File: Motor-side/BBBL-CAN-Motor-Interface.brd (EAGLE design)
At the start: 49.5 x 53.3 mm, 2 parts

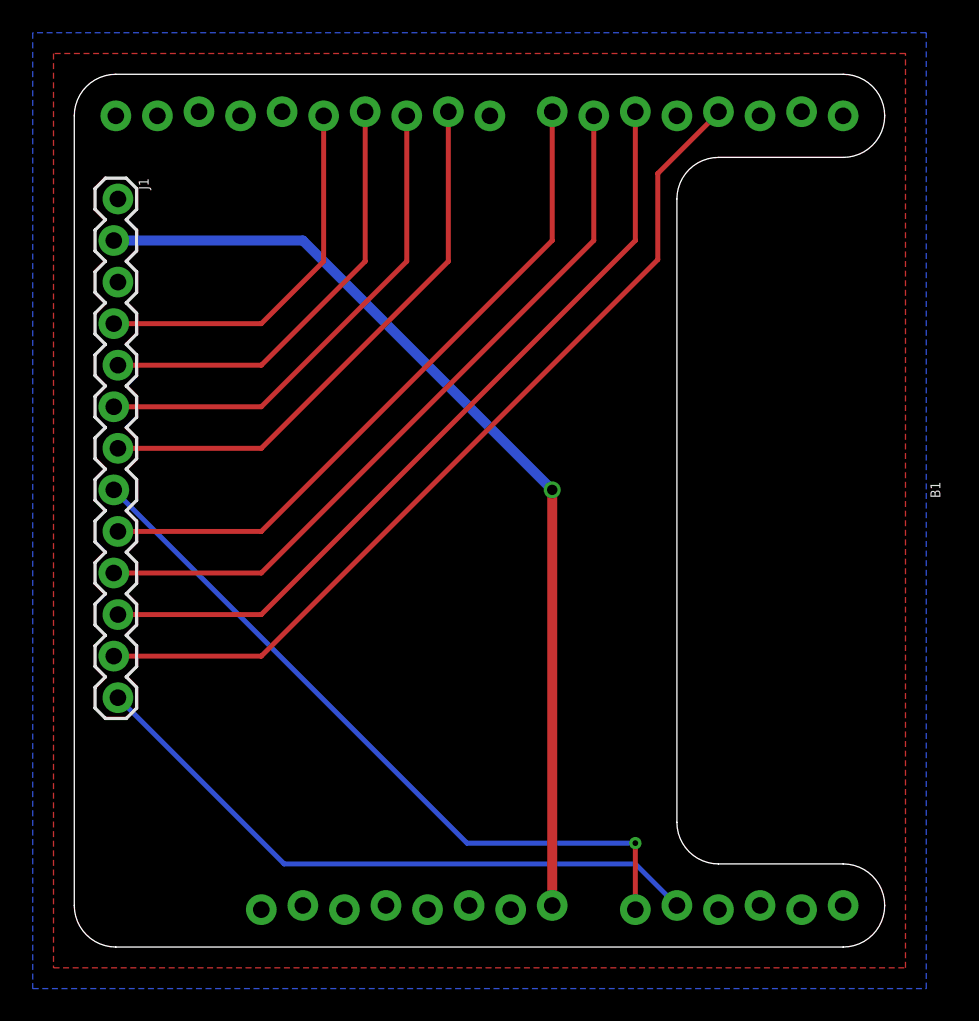
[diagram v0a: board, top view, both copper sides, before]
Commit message: Modified Motor interface for non-interference with the CAN shield.
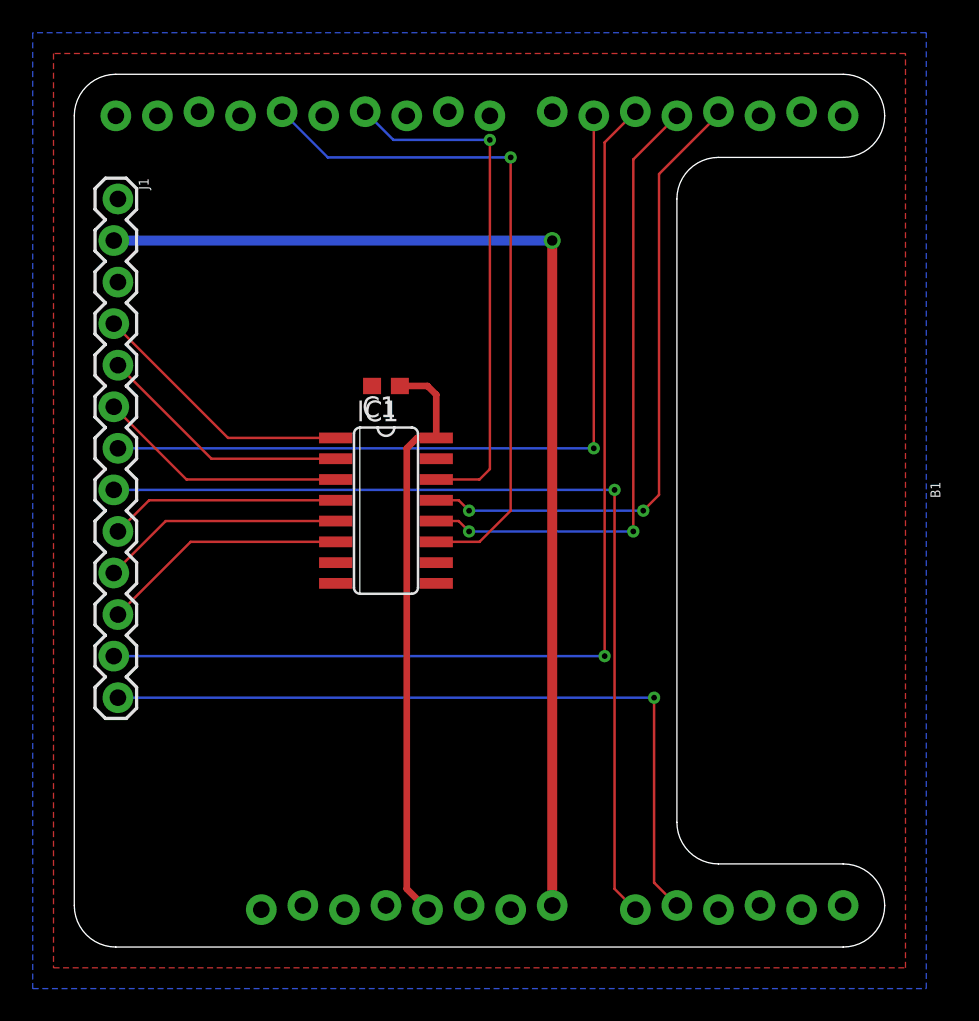
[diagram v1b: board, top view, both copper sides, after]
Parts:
- added C1: 100n, resistor:C0603
- added IC1: 74LS595D, 74xx-us:SO16
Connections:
- new net N$1: B1.D5, J1.12
- new net N$13: B1.D11, IC1.14
- new net N$14: B1.D13, IC1.11
- new net N$15: B1.D4, IC1.12
- new net N$16: B1.5V, C1.1, IC1.16
- net GND: now also C1.2, IC1.8
- net N$10: now also IC1.1, J1.4; no longer B1.D11, J1.5
- net N$11: now also B1.D3, IC1.13; no longer B1.D12, J1.4
- net N$4: now also B1.D6; no longer B1.D9
- net N$5: now also IC1.6, J1.11; no longer B1.D3, J1.12
- net N$6: now also IC1.5, J1.10; no longer B1.D5, J1.11
- net N$7: now also IC1.4, J1.9; no longer B1.D6, J1.10
- net N$8: now also IC1.3, J1.6; no longer B1.D7, J1.9
- net N$9: now also IC1.2, J1.5; no longer B1.D10, J1.6
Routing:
- net N$1: track 0.00 -> 64.1 mm, vias 0 -> 1
- net N$14: track 0.00 -> 42.1 mm, vias 0 -> 1
- net N$15: track 0.00 -> 38.8 mm, vias 0 -> 2
- net N$5: track 53.9 -> 15.2 mm
- net N$16: track 0.00 -> 35.9 mm
- net N$6: track 49.0 -> 14.9 mm
- net N$13: track 0.00 -> 32.0 mm, vias 0 -> 1
- net N$7: track 45.4 -> 14.1 mm
- net N$8: track 41.8 -> 15.4 mm
- net N$11: track 23.3 -> 39.2 mm, vias 0 -> 2
- net N$4: track 34.1 -> 49.4 mm, vias 0 -> 1
- net N$9: track 30.5 -> 15.7 mm
- net N$2: track 44.9 -> 56.8 mm
- net N$10: track 26.9 -> 16.5 mm
- net N$12: track 58.5 -> 67.4 mm
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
